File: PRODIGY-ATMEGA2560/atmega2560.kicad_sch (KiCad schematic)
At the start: 11 parts, among them U1 ATmega2560-8A, U2 TXS0108EPW, Y1 8MHz

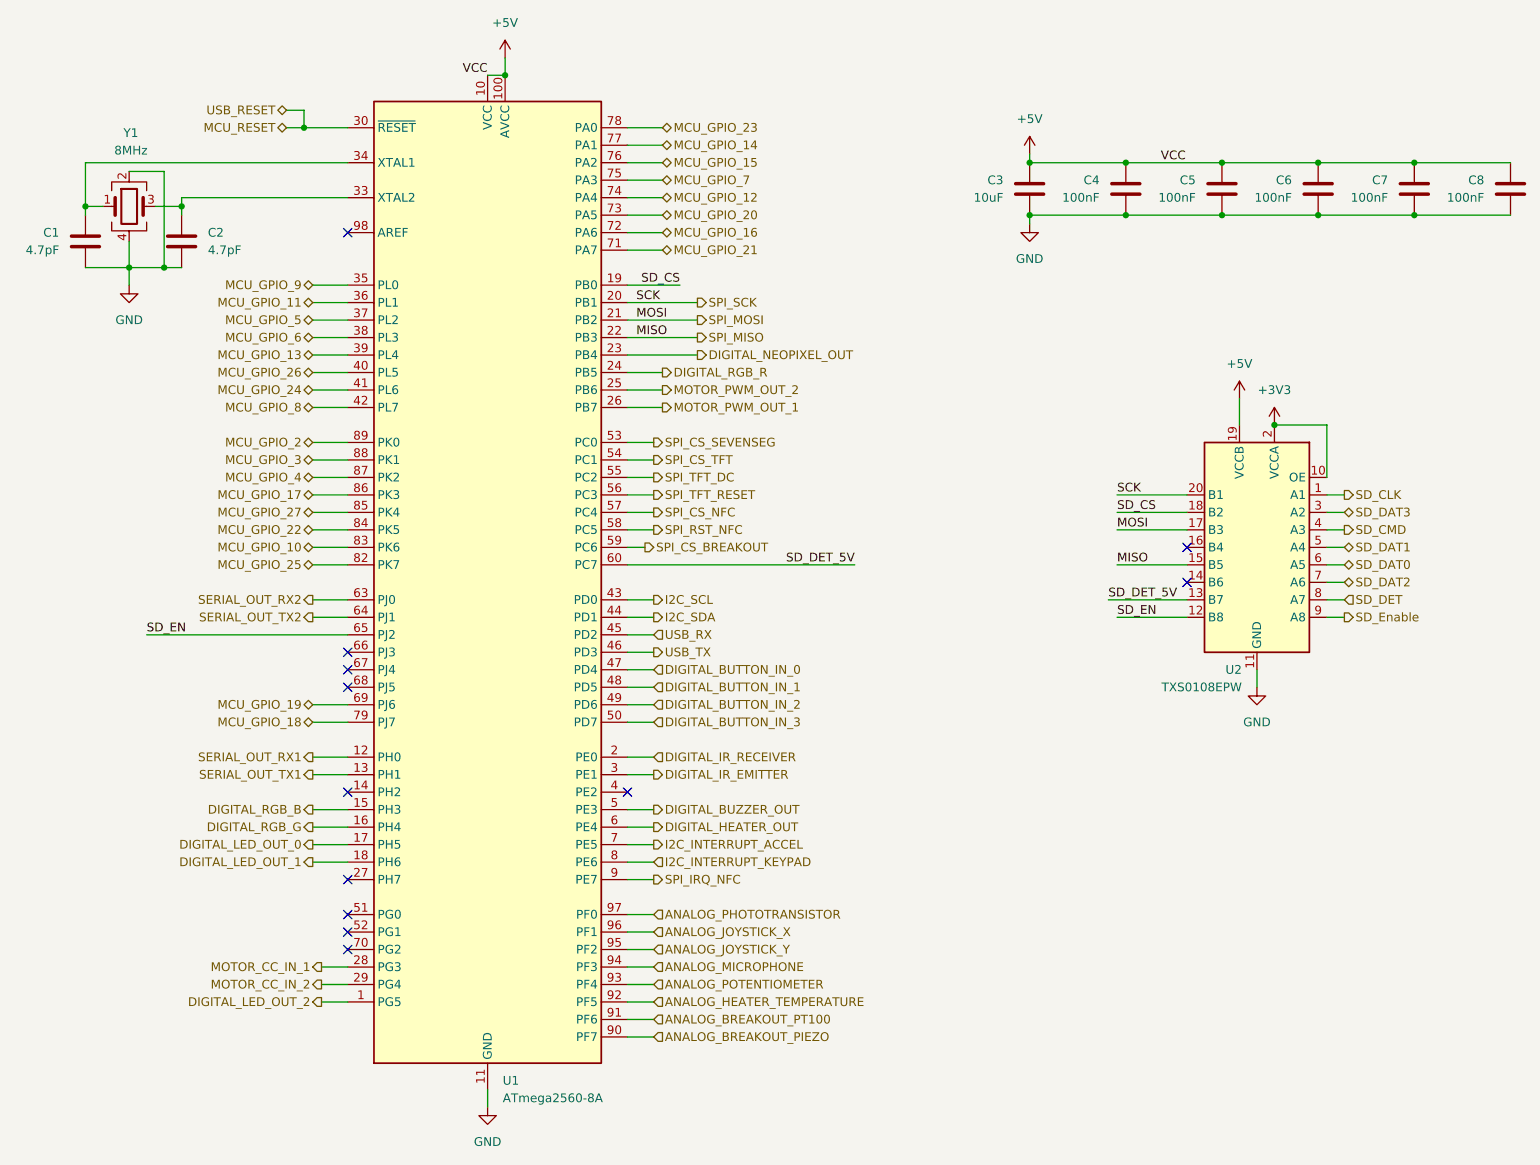
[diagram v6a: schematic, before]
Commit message: Atmega board routing and power planes done. via stitching and labeling is needed
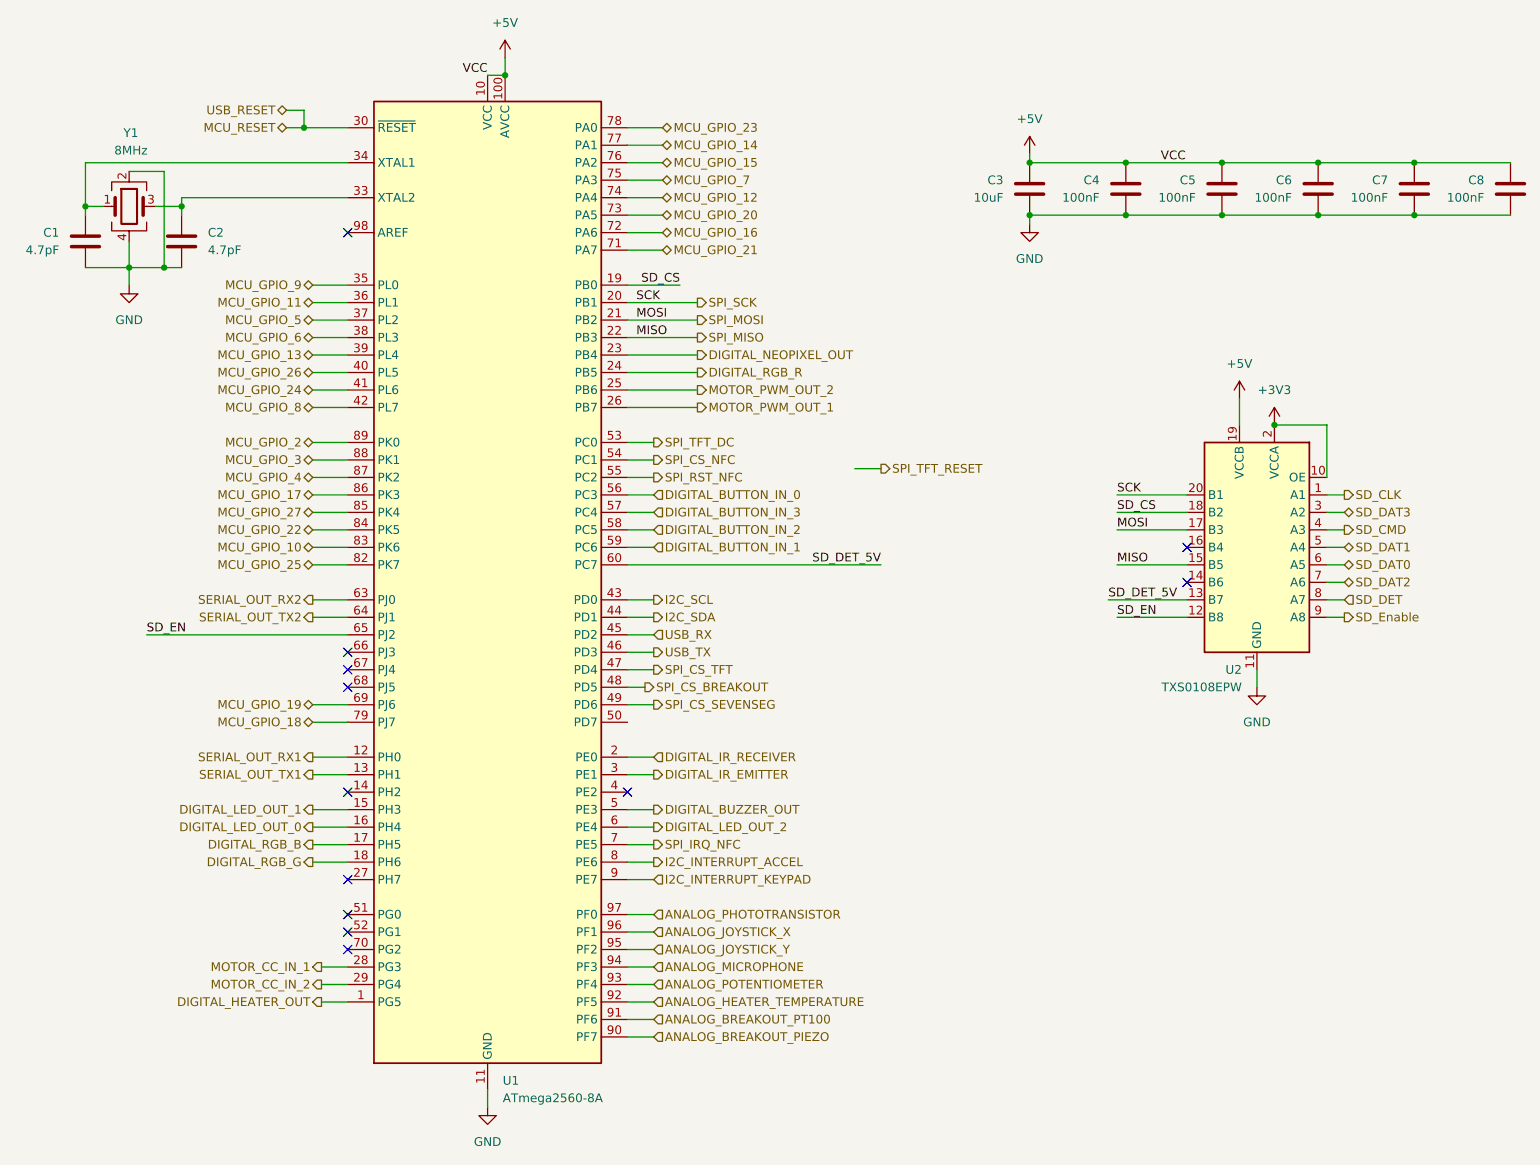
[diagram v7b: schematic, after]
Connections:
- net DIGITAL_BUTTON_IN_0: now also U1.56 (PC3); no longer U1.47 (PD4)
- net DIGITAL_BUTTON_IN_1: now also U1.59 (PC6); no longer U1.48 (PD5)
- net DIGITAL_BUTTON_IN_2: now also U1.58 (PC5); no longer U1.49 (PD6)
- net DIGITAL_BUTTON_IN_3: now also U1.57 (PC4); no longer U1.50 (PD7)
- net DIGITAL_HEATER_OUT: now also U1.1 (PG5); no longer U1.6 (PE4)
- net DIGITAL_LED_OUT_0: now also U1.16 (PH4); no longer U1.17 (PH5)
- net DIGITAL_LED_OUT_1: now also U1.15 (PH3); no longer U1.18 (PH6)
- net DIGITAL_LED_OUT_2: now also U1.6 (PE4); no longer U1.1 (PG5)
- net DIGITAL_RGB_B: now also U1.17 (PH5); no longer U1.15 (PH3)
- net DIGITAL_RGB_G: now also U1.18 (PH6); no longer U1.16 (PH4)
- net I2C_INTERRUPT_ACCEL: now also U1.8 (PE6); no longer U1.7 (PE5)
- net I2C_INTERRUPT_KEYPAD: now also U1.9 (PE7); no longer U1.8 (PE6)
- net SPI_CS_BREAKOUT: now also U1.48 (PD5); no longer U1.59 (PC6)
- net SPI_CS_NFC: now also U1.54 (PC1); no longer U1.57 (PC4)
- net SPI_CS_SEVENSEG: now also U1.49 (PD6); no longer U1.53 (PC0)
- net SPI_CS_TFT: now also U1.47 (PD4); no longer U1.54 (PC1)
- net SPI_IRQ_NFC: now also U1.7 (PE5); no longer U1.9 (PE7)
- net SPI_RST_NFC: now also U1.55 (PC2); no longer U1.58 (PC5)
- net SPI_TFT_DC: now also U1.53 (PC0); no longer U1.55 (PC2)
- net SPI_TFT_RESET: no longer U1.56 (PC3)

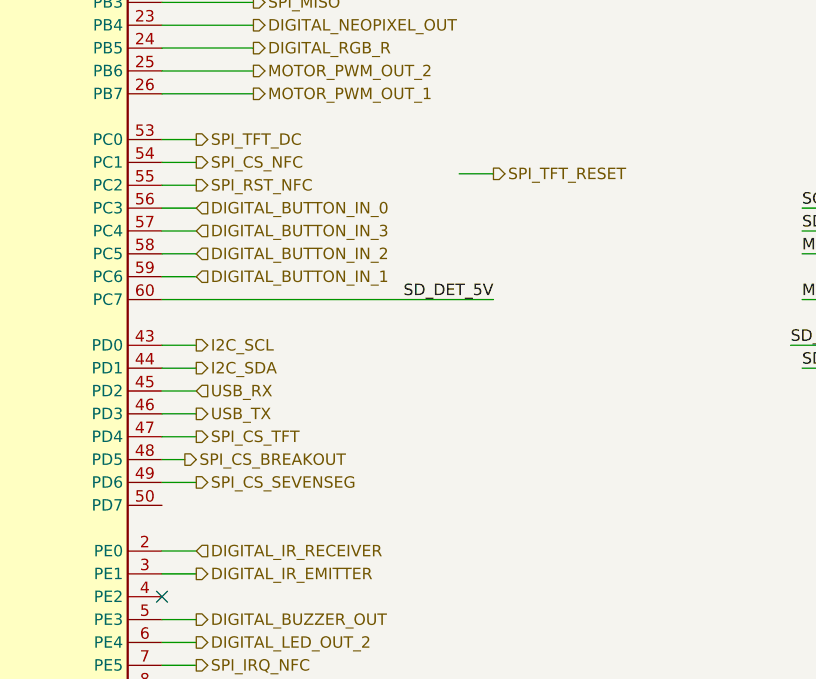
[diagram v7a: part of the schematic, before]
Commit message: DRC ran with 0 errors
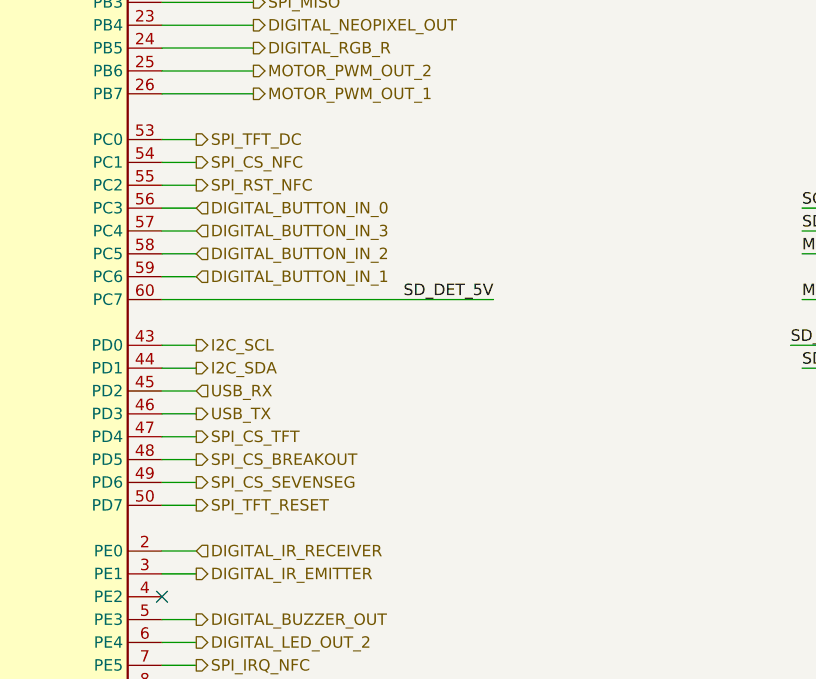
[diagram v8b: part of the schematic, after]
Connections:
- net SPI_TFT_RESET: now also U1.50 (PD7)
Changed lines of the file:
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@@
 	(wire
 		(pts
-			(xy 171.45 87.63) (xy 167.64 87.63)
+			(xy 138.43 124.46) (xy 134.62 124.46)
 		)
 		(stroke
@@
 	(wire
 		(pts
-			(xy 137.16 119.38) (xy 134.62 119.38)
+			(xy 138.43 119.38) (xy 134.62 119.38)
 		)
 		(stroke
@@
 	(hierarchical_label "SPI_TFT_RESET"
 		(shape output)
-		(at 171.45 87.63 0)
+		(at 138.43 124.46 0)
 		(fields_autoplaced yes)
 		(effects
@@
 	(hierarchical_label "SPI_CS_BREAKOUT"
 		(shape output)
-		(at 137.16 119.38 0)
-		(fields_autoplaced yes)
-		(effects
+		(at 138.43 119.38 0)
+		(fields_autoplaced yes)
+		(effects
